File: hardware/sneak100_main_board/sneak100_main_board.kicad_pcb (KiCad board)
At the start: 2 copper layers, 68 x 75 mm, 101 parts, among them J1 Conn_01x06, J10 Conn_01x03, J11 Conn_01x02, J12 Conn_01x04, J13 Conn_01x06, J2 Conn_01x06, J3 Conn_01x06, J4 Conn_01x06, J5 Conn_01x03, J6 Conn_01x02, J7 Conn_01x03, J8 Conn_01x03, J9 Conn_01x03, Q1 Q_PMOS_DGS, Q2 Q_PMOS_DGS, Q3 SFH-313FA, Q4 SFH-313FA, Q5 SFH-313FA, Q6 SFH-313FA, SW1 SW_Push_SPDT, SW2 SW_Push, SW3 SW_Push, SW4 SW_Push, U1 DRV8835, U2 DRV8835, U3 DRV8835, U4 DRV8835, U5 LM1117-3.3, U6 CD4051B, U7 CD4051B, U8 STM32F405RGTx, U9 TSOP4838, Y1 8MHz

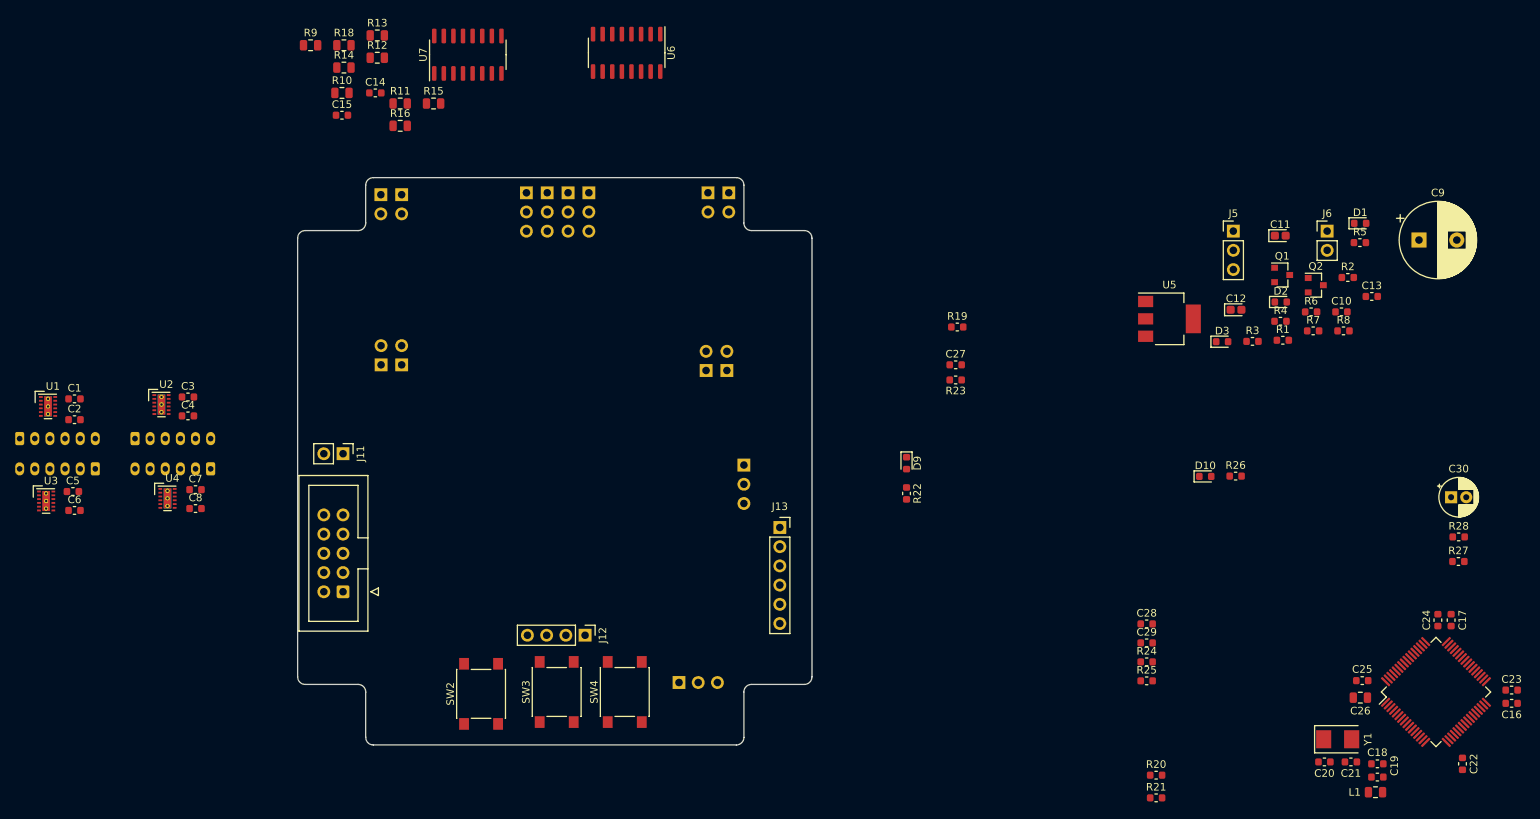
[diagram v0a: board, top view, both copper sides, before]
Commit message: Board interface layout
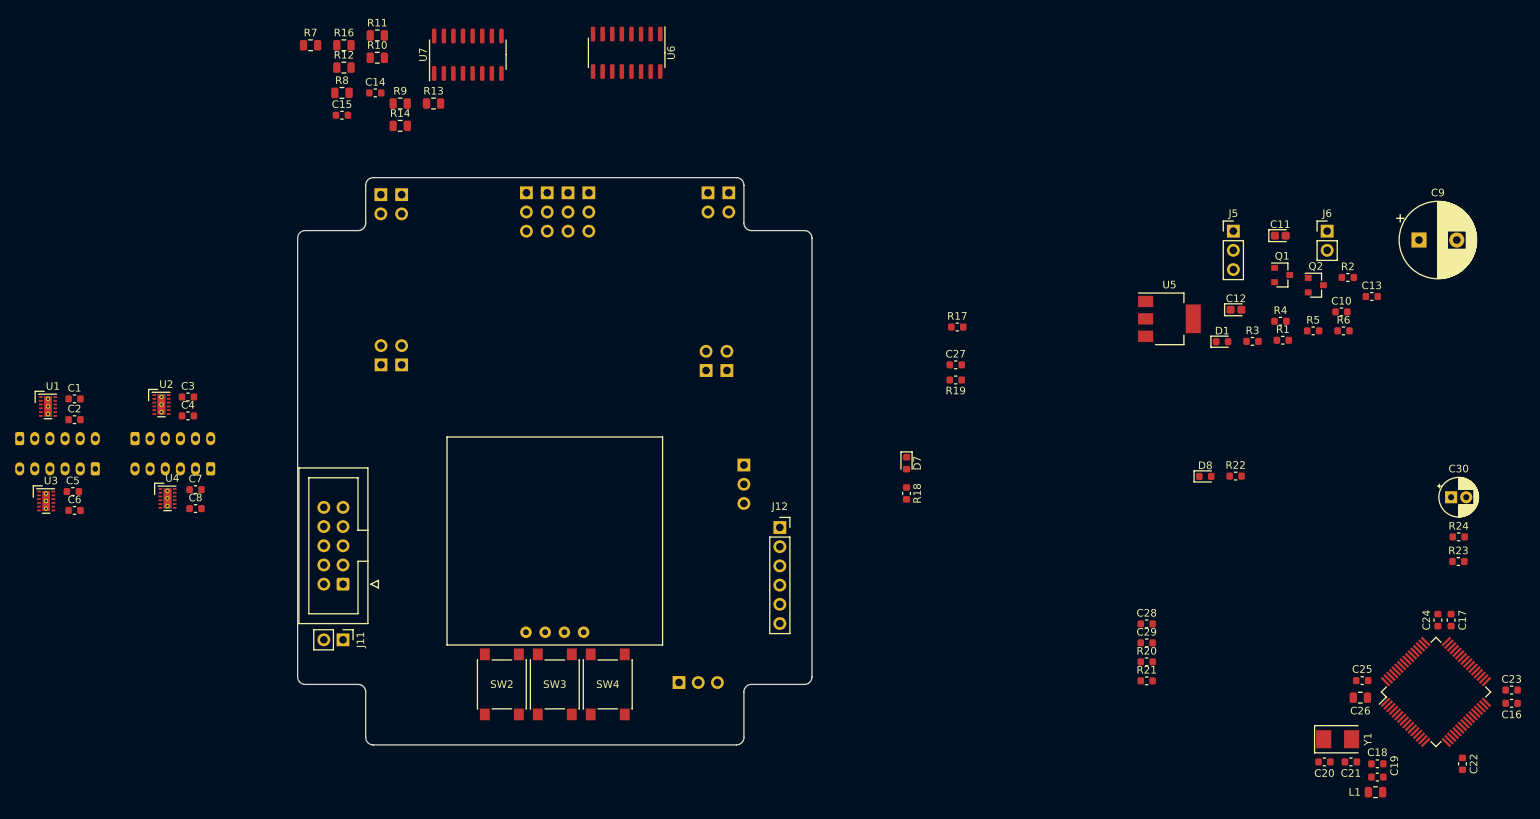
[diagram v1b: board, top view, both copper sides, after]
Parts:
- removed the D1 at (254.2, 47.5)
- removed the D2 at (243.7, 57.9)
- removed the J12 at (151.8, 102.0)
- removed the R20 at (227.2, 120.5)
- removed the R21 at (227.2, 123.5)
- removed the R5 at (254.2, 50.1)
- removed the R6 at (247.7, 59.2)
- added U10: SSD1306, sneak100_lib:SSD1306_module, F.Cu at (147.8, 101.8)
- R4: value R -> 16k
- R5: renamed from R7; value 340 -> 360
- R6: renamed from R8; value R -> 10k
- moved J11 24.6 mm to (119.8, 102.6)
- moved SW2 3.02 mm to (140.8, 108.5)
- moved SW4 2.46 mm to (154.8, 108.5)
- moved SW3 1.03 mm to (147.8, 108.5)
- moved MCU1 1.00 mm to (119.8, 95.2)
- renumbered D3 to D1, D4 to D2, D5 to D3, D6 to D4, D7 to D5, D9 to D7, D10 to D8, J13 to J12, R12 to R10, R13 to R11, R14 to R12, R15 to R13, R16 to R14, R18 to R16, R19 to R17, R22 to R18, R23 to R19, R24 to R20, R25 to R21, R26 to R22, R27 to R23, R28 to R24, R9 to R7, R10 to R8, R11 to R9
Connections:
- R18 pad 2: (no net) -> /interface/LED_RUN
- R22 pad 2: (no net) -> /interface/LED_ERROR
- U8 pad 2: (no net) -> /controller/RECEIVER_OUT
- U8 pad 50: (no net) -> /interface/LED_RUN
- U8 pad 51: (no net) -> /interface/LED_ERROR
- U8 pad 52: (no net) -> /interface/BUTTON_L
- U8 pad 53: (no net) -> /interface/BUTTON_C
- U8 pad 54: /controller/RECEIVER_OUT -> /interface/BUTTON_R

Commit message: PCB first full layout
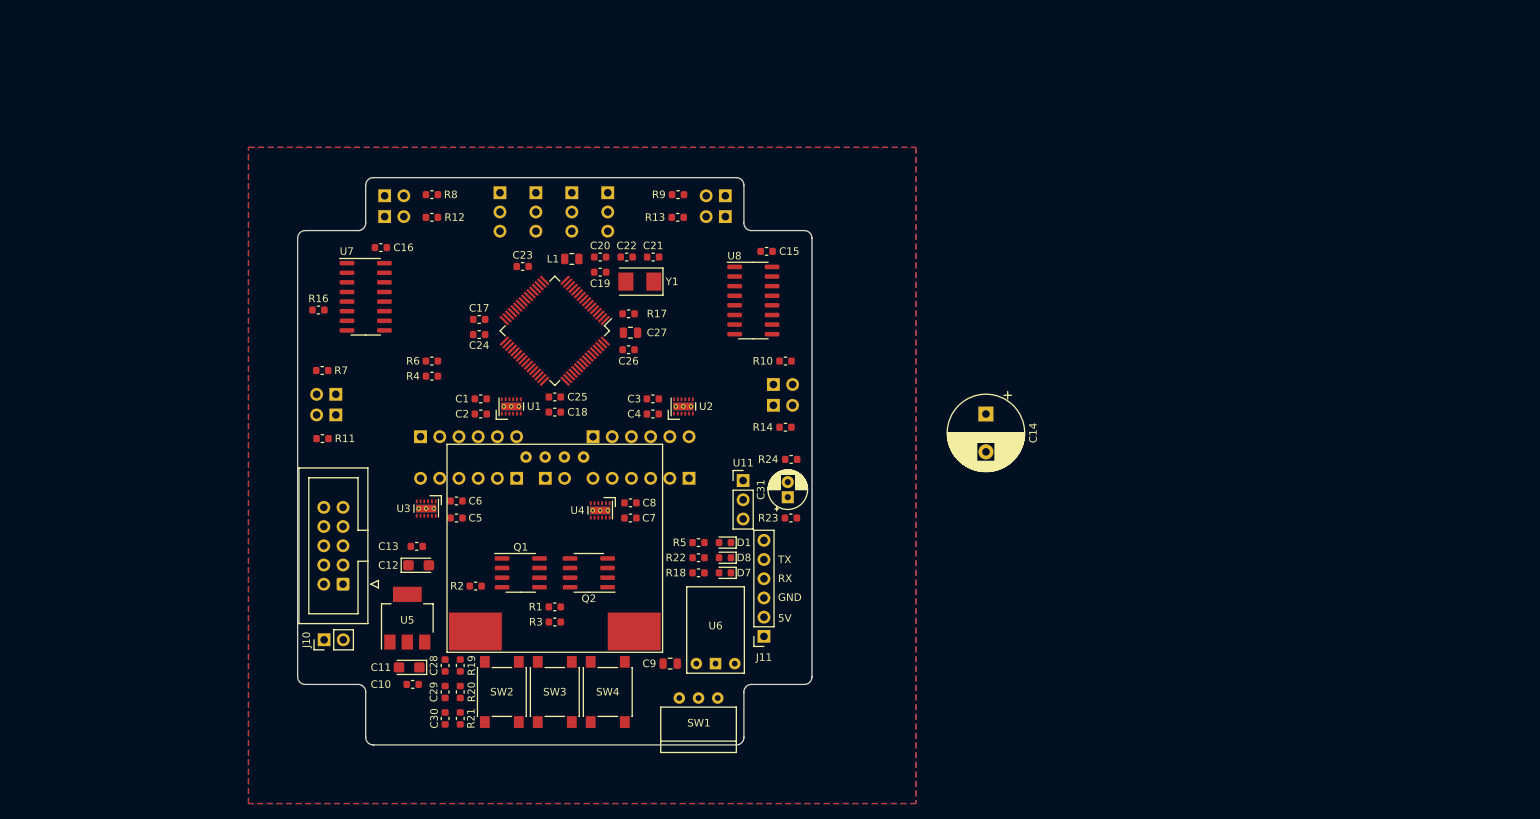
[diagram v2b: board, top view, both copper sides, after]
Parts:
- removed the J5 at (237.5, 48.6)
- added C9: 33uF, Capacitor_SMD:C_0805_2012Metric, F.Cu at (163.0, 105.8)
- added U6: S9V11F5, sneak100_lib:S9V11F5_module, F.Cu at (169.0, 105.8)
- C11, C12: footprint Capacitor_Tantalum_SMD:CP_EIA-1608-10_AVX-L -> Capacitor_Tantalum_SMD:CP_EIA-3216-18_Kemet-A
- J1, J2, J3, J4: footprint Connector_JST:JST_PH_S6B-PH-K_1x06_P2.00mm_Horizontal -> Connector_PinSocket_2.54mm:PinSocket_1x06_P2.54mm_Horizontal
- J5: renamed from J6; footprint Connector_PinHeader_2.54mm:PinHeader_1x02_P2.54mm_Vertical -> Connector_PinHeader_2.54mm:PinHeader_1x02_P2.54mm_Horizontal; moved to B.Cu
- Q1, Q2: value Q_PMOS_DGS -> AO4407; footprint Package_TO_SOT_SMD:SOT-23 -> Package_SO:SOIC-8_3.9x4.9mm_P1.27mm
- R1: value 4k7 -> 10k
- R10, R11, R12, R13, R14, R16, R7, R8, R9: footprint Resistor_SMD:R_0805_2012Metric -> Resistor_SMD:R_0603_1608Metric
- SW1: footprint Connector_PinHeader_2.54mm:PinHeader_1x03_P2.54mm_Vertical -> sneak100_lib:ESP2010_90; moved to F.Cu
- U11: renamed from U9; moved to F.Cu
- moved C17 145.6 mm to (137.8, 60.2), turned to 180 degrees
- moved C24 144.4 mm to (137.8, 62.2), turned to 180 degrees
- moved C23 140.6 mm to (143.5, 53.2), turned to 0 degrees
- moved C10 132.3 mm to (129.0, 108.5), turned to 180 degrees
- moved C13 130.5 mm to (129.5, 90.2)
- moved C11 128.5 mm to (128.5, 106.2), turned to 180 degrees
- moved L1 127.5 mm to (150.0, 52.2)
- moved U9 125.9 mm to (147.8, 61.8), turned to 225 degrees
- moved C20 123.6 mm to (153.8, 52.0), turned to 0 degrees
- moved R2 122.3 mm to (137.3, 95.5), turned to 180 degrees
- moved C18 121.6 mm to (147.8, 72.5), turned to 0 degrees
- moved C19 121.6 mm to (153.8, 54.0), turned to 0 degrees
- moved R6 120.6 mm to (131.5, 65.8), turned to 180 degrees
- moved C25 120.4 mm to (147.8, 70.5), turned to 0 degrees
- moved C22 116.7 mm to (157.2, 52.0), turned to 0 degrees
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- renumbered C9 to C14, C14 to C15, C15 to C16, C16 to C17, C17 to C18, C18 to C19, C19 to C20, C20 to C21, C21 to C22, C22 to C23, C23 to C24, C24 to C25, C25 to C26, C26 to C27, C27 to C28, C28 to C29, C29 to C30, C30 to C31, J11 to J10, J12 to J11, J7 to J6, J8 to J7, J9 to J8, J10 to J9, U6 to U7, U7 to U8, U8 to U9
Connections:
- C14 pad 1: Net-(C9-Pad1) -> SUPPLY
- J1 pad 5: /motors/LF_OUT2 -> /motors/LF_OUT1
- J1 pad 6: /motors/LF_OUT1 -> /motors/LF_OUT2
- J2 pad 5: /motors/RF_OUT2 -> /motors/RF_OUT1
- J2 pad 6: /motors/RF_OUT1 -> /motors/RF_OUT2
- J3 pad 5: /motors/LB_OUT2 -> /motors/LB_OUT1
- J3 pad 6: /motors/LB_OUT1 -> /motors/LB_OUT2
- J4 pad 5: /motors/RB_OUT2 -> /motors/RB_OUT1
- J4 pad 6: /motors/RB_OUT1 -> /motors/RB_OUT2
- J5 pad 1: Net-(C9-Pad1) -> GND
- J5 pad 2: GND -> Net-(J5-Pad2)
- Q1 pad 1: Net-(C9-Pad1) -> Net-(J5-Pad2)
- Q1 pad 2: Net-(Q1-Pad2) -> Net-(J5-Pad2)
- Q1 pad 3: Net-(Q1-Pad3) -> Net-(J5-Pad2)
- Q2 pad 2: Net-(Q2-Pad2) -> SUPPLY
- Q2 pad 3: Net-(Q1-Pad3) -> SUPPLY
- R1 pad 1: Net-(Q1-Pad3) -> Net-(Q1-Pad5)
- R1 pad 2: Net-(Q2-Pad2) -> Net-(Q2-Pad4)
- R2 pad 1: Net-(Q1-Pad2) -> Net-(Q1-Pad4)
- R3 pad 1: Net-(Q2-Pad2) -> Net-(Q2-Pad4)
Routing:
- added copper zone on B.Cu, net GND
- added copper zone on F.Cu, net GND
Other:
- board text added: "5V"
- board text added: "GND"
- board text added: "RX"
- board text added: "TX"

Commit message: More space in top hull and schematic fix
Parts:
- removed the J10 at (117.2, 102.6)
- removed R24: 10k, Resistor_SMD:R_0603_1608Metric
- added JP1: Jumper_2_Open, Connector_PinHeader_2.54mm:PinHeader_2x01_P2.54mm_Vertical, F.Cu at (117.2, 102.8)
- renumbered J11 to J10
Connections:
- C31 pad 1: +3V3 -> Net-(C31-Pad1)
- R23 pad 2: Net-(R23-Pad2) -> Net-(C31-Pad1)
- U11 pad 3: Net-(R23-Pad2) -> Net-(C31-Pad1)
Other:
- board text added: "3.3V"
- board text added: "NC"
- board text added: "RST"
- board text added: "SWCLK"
- board text added: "SWDIO"

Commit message: bluetooth en & status connection
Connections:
- J10 pad 1: (no net) -> /controller/BLUETOOTH_EN
- J10 pad 6: (no net) -> /controller/BLUETOOTH_STATUS
- U9 pad 20: (no net) -> /controller/BLUETOOTH_EN
- U9 pad 21: (no net) -> /controller/BLUETOOTH_STATUS

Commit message: First routes on PCB
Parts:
- moved C3 1.20 mm to (160.7, 69.5)
- moved C4 1.20 mm to (160.7, 71.5)
- moved U2 1.20 mm to (164.8, 70.5)
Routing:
- net Net-(J5-Pad2): track 0.00 -> 16.2 mm
- net /motors/RF_OUT1: track 0.00 -> 9.78 mm
- net /motors/RF_OUT2: track 0.00 -> 9.44 mm, vias 0 -> 1
- net SUPPLY: vias 0 -> 12
- added copper zone on F.Cu, net Net-(J5-Pad2)
- added copper zone on F.Cu, net Net-(Q1-Pad5)
- added copper zone on B.Cu, net SUPPLY
- added copper zone on F.Cu, net SUPPLY
- removed copper zone on B.Cu, net GND
- removed copper zone on F.Cu, net GND
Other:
- board text added: "EN"
- board text added: "STATUS"
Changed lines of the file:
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@@
     (thickness 1.6)
     (drawings 50)
-    (tracks 0)
+    (tracks 28)
     (zones 0)
     (modules 95)
@@
   )
   (setup
-    (last_trace_width 0.25)
+    (last_trace_width 2)
+    (user_trace_width 0.3)
+    (user_trace_width 0.4)
+    (user_trace_width 0.5)
+    (user_trace_width 0.6)
+    (user_trace_width 0.7)
+    (user_trace_width 1)
+    (user_trace_width 2)
     (trace_clearance 0.2)
     (zone_clearance 0.508)
@@
     (mod_text_size 1 1)
     (mod_text_width 0.15)
-    (pad_size 1.524 1.524)
-    (pad_drill 0.762)
+    (pad_size 0.5 0.25)
+    (pad_drill 0)
     (pad_to_mask_clearance 0.05)
     (aux_axis_origin 0 0)
@@
     (tags "SOIC SO")
     (attr smd)
-    (fp_text reference Q2 (at 0 -3.4) (layer F.SilkS)
+    (fp_text reference Q2 (at -2.65 -3.45) (layer F.SilkS)
       (effects (font (size 1 1) (thickness 0.15)))
     )
@@
     (tags "SOIC SO")
     (attr smd)
-    (fp_text reference Q1 (at 0 -3.4) (layer F.SilkS)
+    (fp_text reference Q1 (at -2.85 -3.45) (layer F.SilkS)
       (effects (font (size 1 1) (thickness 0.15)))
     )
@@
     (descr "Through hole angled socket strip, 1x06, 2.54mm pitch, 8.51mm socket length, single row (from Kicad 4.0.7), script generated")
     (tags "Through hole angled socket strip THT 1x06 2.54mm single row")
+    (zone_connect 2)
     (fp_text reference J2 (at -4.38 2.77 90) (layer B.SilkS)
       (effects (font (size 1 1) (thickness 0.15)) (justify mirror))
@@
     )
     (pad 6 thru_hole oval (at 0 -12.7 270) (size 1.7 1.7) (drill 1) (layers *.Cu *.Mask)
-      (net 12 /motors/RF_OUT2))
+      (net 12 /motors/RF_OUT2) (zone_connect 2))
     (pad 5 thru_hole oval (at 0 -10.16 270) (size 1.7 1.7) (drill 1) (layers *.Cu *.Mask)
-      (net 11 /motors/RF_OUT1))
+      (net 11 /motors/RF_OUT1) (zone_connect 2))
     (pad 4 thru_hole oval (at 0 -7.62 270) (size 1.7 1.7) (drill 1) (layers *.Cu *.Mask)
-      (net 2 +3V3))
+      (net 2 +3V3) (zone_connect 2))
     (pad 3 thru_hole oval (at 0 -5.08 270) (size 1.7 1.7) (drill 1) (layers *.Cu *.Mask)
-      (net 33 /controller/RF_A))
+      (net 33 /controller/RF_A) (zone_connect 2))
     (pad 2 thru_hole oval (at 0 -2.54 270) (size 1.7 1.7) (drill 1) (layers *.Cu *.Mask)
-      (net 34 /controller/RF_B))
+      (net 34 /controller/RF_B) (zone_connect 2))
     (pad 1 thru_hole rect (at 0 0 270) (size 1.7 1.7) (drill 1) (layers *.Cu *.Mask)
-      (net 1 GND))
+      (net 1 GND) (zone_connect 2))
     (model ${KISYS3DMOD}/Connector_PinSocket_2.54mm.3dshapes/PinSocket_1x06_P2.54mm_Horizontal.wrl
       (at (xyz 0 0 0))
@@
   )
   (module Package_SON:WSON-12-1EP_3x2mm_P0.5mm_EP1x2.65_ThermalVias (layer F.Cu)
-    (at 164.75 71.75 90)
+    (at 164.75 70.55 90)
     (descr "WSON-12 http://www.ti.com/lit/ds/symlink/lm27762.pdf")
     (tags WSON-12)
@@
       (net 1 GND))
     (pad 5 smd rect (at -0.95 0.75 90) (size 0.5 0.25) (layers F.Cu F.Paste F.Mask)
-      (net 12 /motors/RF_OUT2))
+      (net 12 /motors/RF_OUT2) (zone_connect 2))
     (pad 4 smd rect (at -0.95 0.25 90) (size 0.5 0.25) (layers F.Cu F.Paste F.Mask)
       (net 11 /motors/RF_OUT1))
     (pad 3 smd rect (at -0.95 -0.25 90) (size 0.5 0.25) (layers F.Cu F.Paste F.Mask)
-      (net 12 /motors/RF_OUT2))
+      (net 12 /motors/RF_OUT2) (zone_connect 2))
     (pad 2 smd rect (at -0.95 -0.75 90) (size 0.5 0.25) (layers F.Cu F.Paste F.Mask)
       (net 11 /motors/RF_OUT1))
@@
   )
   (module Capacitor_SMD:C_0603_1608Metric (layer F.Cu)
-    (at 160.7125 72.75 180)
+    (at 160.7125 71.55 180)
     (descr "Capacitor SMD 0603 (1608 Metric), square (rectangular) end terminal, IPC_7351 nominal, (Body size source: http://www.tortai-tech.com/upload/download/2011102023233369053.pdf), generated with kicad-footprint-generator")
     (tags capacitor)
@@
   )
   (module Capacitor_SMD:C_0603_1608Metric (layer F.Cu)
-    (at 160.7125 70.75 180)
+    (at 160.7125 69.55 180)
     (descr "Capacitor SMD 0603 (1608 Metric), square (rectangular) end terminal, IPC_7351 nominal, (Body size source: http://www.tortai-tech.com/upload/download/2011102023233369053.pdf), generated with kicad-footprint-generator")
     (tags capacitor)
@@
     )
   )
-  (gr_text NC (at 177.25 89.5) (layer F.SilkS)
+  (gr_text STATUS (at 177.25 89.5) (layer F.SilkS)
     (effects (font (size 1 1) (thickness 0.15)) (justify left))
   )
-  (gr_text NC (at 177.25 102.25) (layer F.SilkS)
+  (gr_text EN (at 177.25 102.25) (layer F.SilkS)
     (effects (font (size 1 1) (thickness 0.15)) (justify left))
   )
@@
   (gr_line (start 171.75 116.5) (end 123.75 116.5) (layer Edge.Cuts) (width 0.05))
   (gr_line (start 123.75 41.5) (end 171.75 41.5) (layer Edge.Cuts) (width 0.05))
-  (zone (net 1) (net_name GND) (layer F.Cu) (hatch edge 0.508)
-    (connect_pads (clearance 0.508))
+  (segment (start 165 73.71) (end 162.96 75.75) (width 0.3) (layer F.Cu) (net 11))
+  (segment (start 165 71.5) (end 165 73.71) (width 0.3) (layer F.Cu) (net 11))
+  (segment (start 162.96 75.75) (end 162.96 73.34) (width 0.3) (layer F.Cu) (net 11))
+  (segment (start 164 72.3) (end 164 71.5) (width 0.3) (layer F.Cu) (net 11))
+  (segment (start 162.96 73.34) (end 164 72.3) (width 0.3) (layer F.Cu) (net 11))
+  (segment (start 165.5 71.5) (end 165.5 75.75) (width 0.3) (layer F.Cu) (net 12))
+  (segment (start 164.5 71.5) (end 164.5 72.7) (width 0.3) (layer F.Cu) (net 12))
+  (segment (start 164.5 72.7) (end 164.5 73) (width 0.3) (layer F.Cu) (net 12))
+  (segment (start 164.5 73) (end 163.95 73.55) (width 0.3) (layer F.Cu) (net 12))
+  (segment (start 163.95 73.55) (end 163.9 73.6) (width 0.3) (layer F.Cu) (net 12))
+  (via (at 163.95 73.55) (size 0.8) (drill 0.4) (layers F.Cu B.Cu) (net 12))
+  (segment (start 165.5 75.1) (end 163.95 73.55) (width 0.7) (layer B.Cu) (net 12))
+  (segment (start 165.5 75.75) (end 165.5 75.1) (width 0.7) (layer B.Cu) (net 12))
+  (via (at 159.1 91.9) (size 0.8) (drill 0.4) (layers F.Cu B.Cu) (net 58))
+  (via (at 158 91.9) (size 0.8) (drill 0.4) (layers F.Cu B.Cu) (net 58))
+  (via (at 159.1 93) (size 0.8) (drill 0.4) (layers F.Cu B.Cu) (net 58))
+  (via (at 158 93) (size 0.8) (drill 0.4) (layers F.Cu B.Cu) (net 58))
+  (via (at 159.1 94.1) (size 0.8) (drill 0.4) (layers F.Cu B.Cu) (net 58))
+  (via (at 158 94.1) (size 0.8) (drill 0.4) (layers F.Cu B.Cu) (net 58))
+  (via (at 159.1 95.2) (size 0.8) (drill 0.4) (layers F.Cu B.Cu) (net 58))
+  (via (at 158 95.2) (size 0.8) (drill 0.4) (layers F.Cu B.Cu) (net 58))
+  (via (at 156.9 91.9) (size 0.8) (drill 0.4) (layers F.Cu B.Cu) (net 58))
+  (via (at 156.9 93) (size 0.8) (drill 0.4) (layers F.Cu B.Cu) (net 58))
+  (via (at 156.9 94.1) (size 0.8) (drill 0.4) (layers F.Cu B.Cu) (net 58))
+  (via (at 156.9 95.2) (size 0.8) (drill 0.4) (layers F.Cu B.Cu) (net 58))
+  (segment (start 149.04 81.25) (end 149.04 83.96) (width 2) (layer F.Cu) (net 74))
+  (segment (start 149.04 83.96) (end 143.1 89.9) (width 2) (layer F.Cu) (net 74))
+  (segment (start 143.1 89.9) (end 143.1 95) (width 2) (layer F.Cu) (net 74))
+  (zone (net 75) (net_name "Net-(Q1-Pad5)") (layer F.Cu) (hatch edge 0.508)
+    (connect_pads yes (clearance 0.508))
+    (min_thickness 0.254)
+    (fill yes (arc_segments 32) (thermal_gap 0.508) (thermal_bridge_width 0.508))
+    (polygon
+      (pts
+        (xy 150.8 96.1) (xy 147.8 96.1) (xy 144.6 96.1) (xy 144.6 91.3) (xy 150.8 91.3)
+      )
+    )
+  )
+  (zone (net 74) (net_name "Net-(J5-Pad2)") (layer F.Cu) (hatch edge 0.508)
+    (connect_pads yes (clearance 0.508))
+    (min_thickness 0.254)
+    (fill yes (arc_segments 32) (thermal_gap 0.508) (thermal_bridge_width 0.508))
+    (polygon
+      (pts
+        (xy 144.1 91.6) (xy 144.1 96.1) (xy 142 96.1) (xy 142 95) (xy 139.6 95)
+        (xy 139.6 91.3) (xy 144.1 91.3)
+      )
+    )
+  )
+  (zone (net 58) (net_name SUPPLY) (layer F.Cu) (hatch edge 0.508)
+    (connect_pads yes (clearance 0.508))
     (min_thickness 0.254)
     (fill yes (arc_segments 32) (thermal_gap 0.508) (thermal_bridge_width 0.508))
     (polygon
       (pts
-        (xy 195.5 124.25) (xy 107.25 124.25) (xy 107.25 37.5) (xy 195.5 37.5)
+        (xy 159.6 96.1) (xy 153.5 96.1) (xy 153.5 92.6) (xy 156 92.6) (xy 156 91.4)
+        (xy 159.6 91.4)
       )
     )
   )
-  (zone (net 1) (net_name GND) (layer B.Cu) (hatch edge 0.508)
-    (connect_pads (clearance 0.508))
+  (zone (net 58) (net_name SUPPLY) (layer B.Cu) (hatch edge 0.508)
+    (connect_pads yes (clearance 0.508))
     (min_thickness 0.254)
     (fill yes (arc_segments 32) (thermal_gap 0.508) (thermal_bridge_width 0.508))
     (polygon
       (pts
-        (xy 195.5 124.25) (xy 107.25 124.25) (xy 107.25 37.5) (xy 195.5 37.5)
+        (xy 128.2 87.1) (xy 159.6 87.1) (xy 159.6 96.1) (xy 156.4 96.1) (xy 156.4 90.1)
+        (xy 124.5 90.1) (xy 124.5 69.7) (xy 128.2 69.7)
       )
     )
